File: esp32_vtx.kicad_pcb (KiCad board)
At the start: 4 copper layers, 20.1 x 23.3 mm, 33 parts, among them J1 Conn_01x24_MountingPin, J2 Conn_01x05, U1 AMS1117-3.3, U2 ESP-PSRAM32, U3 ESP32-PICO-D4, U4 MKDV4GCL-AB, U5 XC6206PxxxMR, U6 XC6206PxxxMR

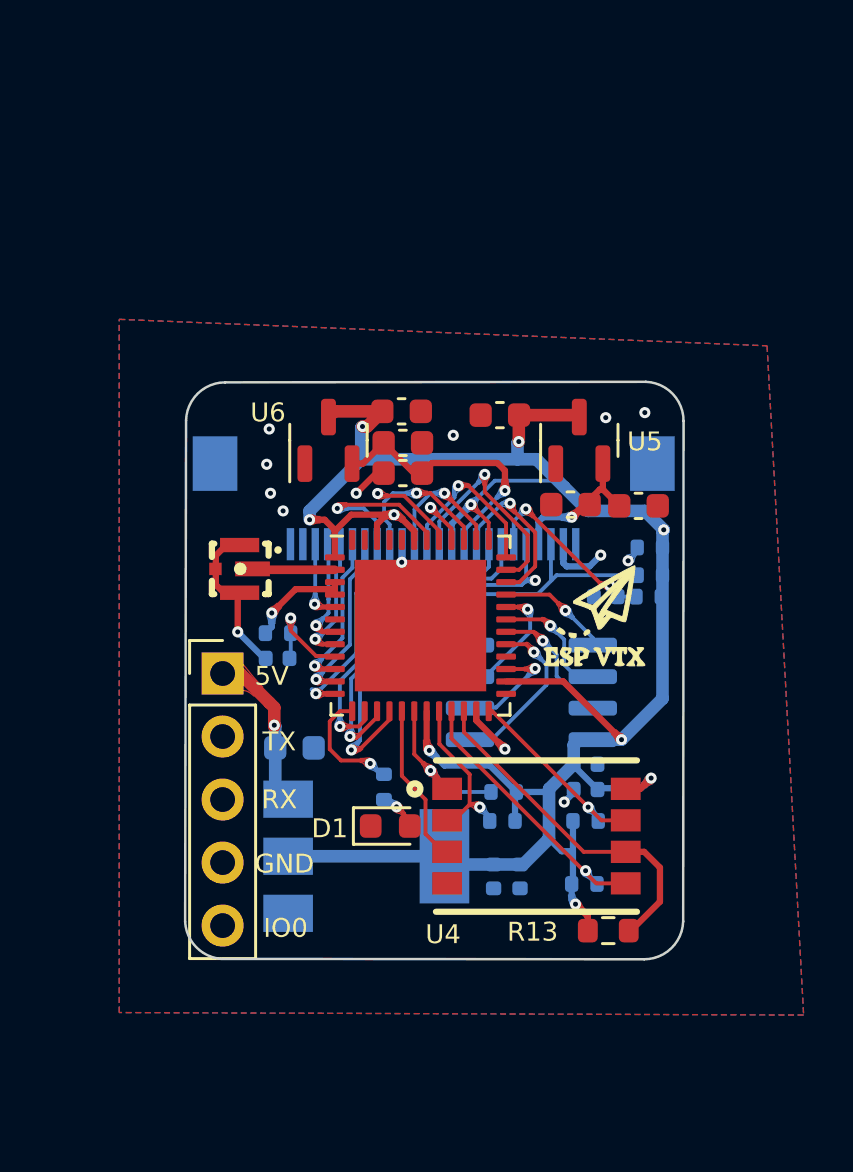
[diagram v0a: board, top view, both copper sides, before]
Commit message: add cap near pclk, change package of res and cap to 0603
Signed-off-by: huangzzk <huangcmzzk@gmail.com>
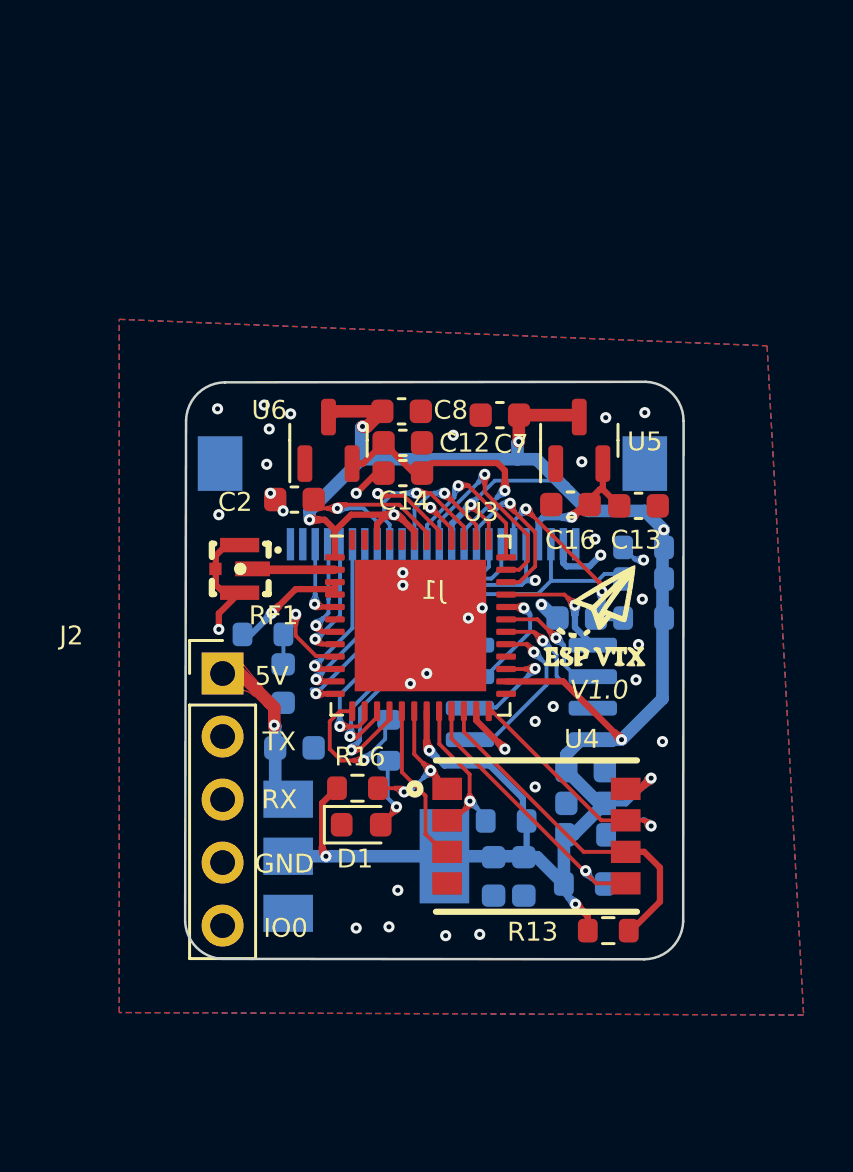
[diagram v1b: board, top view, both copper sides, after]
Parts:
- added C2: 0.1uF, Capacitor_SMD:C_0603_1608Metric, F.Cu at (126.7, 92.4)
- C10, C11, C15, C5, C6, C9: footprint Capacitor_SMD:C_0402_1005Metric -> Capacitor_SMD:C_0603_1608Metric
- R1, R11, R12, R14, R15, R17, R18, R9: footprint Resistor_SMD:R_0402_1005Metric -> Resistor_SMD:R_0603_1608Metric
- R16: footprint Resistor_SMD:R_0402_1005Metric -> Resistor_SMD:R_0603_1608Metric; moved to F.Cu
- U2: value ESP-PSRAM32 -> IS25WP032
- U5: value XC6206PxxxMR -> XC6206-2.8V
- U6: value XC6206PxxxMR -> XC6206-1.2V
- moved R16 5.89 mm to (129.2, 104.0), turned to 0 degrees
- moved R12 1.89 mm to (130.5, 102.1)
- moved C9 1.45 mm to (138.1, 97.1)
- moved D1 1.17 mm to (129.4, 105.5)
- moved C11 1.04 mm to (126.2, 99.8), turned to -90 degrees
- moved R1 0.89 mm to (140.8, 97.1)
- moved R11 0.61 mm to (125.4, 97.8)
- moved C15 0.56 mm to (138.4, 104.6)
- moved R15 0.56 mm to (138.4, 105.9)
- moved R9 0.30 mm to (140.8, 95.6)
- moved R14 0.25 mm to (140.8, 94.3)
- moved C10 0.25 mm to (138.4, 103.3)
- moved C5 0.15 mm to (135.9, 107.5)
- moved R17 0.15 mm to (135.2, 105.3)
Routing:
- net +3V3: track 104.9 -> 108.3 mm, vias 11 -> 12
- net /SD_DATA1: track 8.07 -> 10.6 mm
- net /SDA: track 20.7 -> 18.2 mm
- net /VS: track 13.9 -> 12.1 mm
- net Net-(D1-Pad2): track 1.41 -> 3.12 mm
- net /PWDN: track 12.3 -> 10.9 mm
- net /SCL: track 20.7 -> 19.5 mm
- net /PCLK: track 7.17 -> 8.27 mm
- net Net-(R12-Pad1): track 4.80 -> 5.82 mm
- net /EN: track 4.37 -> 5.28 mm
- net /RESET: track 7.61 -> 8.49 mm
- net GND: track 12.3 -> 11.6 mm, vias 12 -> 34
- net /SD_DATA2: track 6.47 -> 6.22 mm, vias 1 -> 2
- net (no net): vias 0 -> 1
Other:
- board text added: "V1.0"

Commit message: v1.1 tested.
Signed-off-by: huangzzk <huangcmzzk@gmail.com>
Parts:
- removed C6: 0.1uF, Capacitor_SMD:C_0603_1608Metric
- added C3: 100uF, Capacitor_Tantalum_SMD:CP_EIA-3216-18_Kemet-A, B.Cu at (137.9, 107.7)
- added R2: 0R, Resistor_SMD:R_0603_1608Metric, F.Cu at (123.9, 108.9)
- added R3: 0R, Resistor_SMD:R_0603_1608Metric, B.Cu at (123.9, 109.2)
- added SW1: SW_SPST, Button_Switch_SMD:SW_SPST_B3U-1000P, F.Cu at (128.2, 109.1)
- added SW2: SW_SPST, Button_Switch_SMD:SW_SPST_B3U-1000P, F.Cu at (128.2, 106.1)
- C2: value 0.1uF -> 15pF; moved to B.Cu
- J2: value Conn_01x05 -> Conn_01x04; footprint Connector_PinHeader_2.54mm:PinHeader_1x05_P2.54mm_Vertical -> Connector_PinHeader_2.54mm:PinHeader_1x04_P2.54mm_Vertical
- R13, R16: moved to B.Cu
- moved C2 5.61 mm to (131.1, 95.8), turned to 0 degrees
- moved D1 3.04 mm to (126.8, 103.8)
- moved R16 2.99 mm to (131.5, 102.1), turned to -90 degrees
- moved R15 2.24 mm to (140.6, 106.4)
- moved R18 2.24 mm to (140.6, 107.9)
- moved R13 1.31 mm to (140.6, 109.4)
- moved C14 0.56 mm to (131.1, 90.7), turned to 0 degrees
- moved C12 0.46 mm to (131.1, 89.6)
- moved R12 0.46 mm to (130.0, 102.1)
- moved U6 0.46 mm to (128.1, 89.5)
- moved C8 0.36 mm to (131.0, 88.4)
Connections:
- C12 pad 2: GND -> GNDD
- C13 pad 2: GND -> GNDA
- C14 pad 2: GND -> GNDD
- C16 pad 2: GND -> GNDA
- C2 pad 2: GND -> GNDD
- J1 pad 10: GND -> GNDD
- J1 pad 23: GND -> GNDA
- U5 pad 1: GND -> GNDA
- U6 pad 1: GND -> GNDD
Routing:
- net GNDA: track 0.00 -> 37.4 mm, vias 0 -> 2
- net GNDD: track 0.00 -> 31.7 mm, vias 0 -> 2
- net /SD_DATA0: track 14.1 -> 24.5 mm, vias 0 -> 1
- net /GPIO0: track 16.3 -> 8.40 mm, vias 1 -> 2
- net +3V3: track 108.3 -> 104.8 mm, vias 12 -> 8
- net /D7: track 6.26 -> 8.53 mm
- net +1V2: track 11.0 -> 13.0 mm, vias 1 -> 2
- net /SD_DATA2: track 6.22 -> 4.44 mm, vias 2 -> 1
- net /PCLK: track 8.27 -> 9.60 mm, vias 1 -> 2
- net /D8: track 5.30 -> 6.63 mm
- net /TX: track 17.4 -> 18.7 mm
- net /SCL: track 19.5 -> 20.7 mm
- net /SD_CMD: track 11.3 -> 12.5 mm
- net /SD_DATA1: track 10.6 -> 9.48 mm
- net /D6: track 7.05 -> 8.07 mm
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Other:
- board text added: "G"
- board text added: "R"
- board text added: "T"
- board text added: "V1.1"
- board text removed: "GND"
- board text removed: "IO0"
- board text removed: "RX"
- board text removed: "TX"
- board text removed: "V1.0"

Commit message: update
Signed-off-by: huangzzk <huangcmzzk@gmail.com>
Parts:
- removed R2, R3: 0R, Resistor_SMD:R_0603_1608Metric
- added ?: , , F.Cu at (132.4, 78.9)
- added C17: 10u, Capacitor_SMD:C_0603_1608Metric, F.Cu at (130.7, 92.0)
- added C18: 10u, Capacitor_SMD:C_0603_1608Metric, F.Cu at (135.3, 92.2)
- added C19: 10u, Capacitor_SMD:C_0603_1608Metric, B.Cu at (127.5, 90.8)
- added C4: 10u, Capacitor_SMD:C_0603_1608Metric, F.Cu at (126.9, 93.0)
- added C6: 10u, Capacitor_SMD:C_0603_1608Metric, F.Cu at (129.0, 92.0)
- added H1: MountingHole, MountingHole:MountingHole_2.2mm_M2, F.Cu at (124.4, 111.4)
- added H2: MountingHole, MountingHole:MountingHole_2.2mm_M2, F.Cu at (124.4, 87.7)
- added H3: MountingHole, MountingHole:MountingHole_2.2mm_M2, F.Cu at (140.3, 111.2)
- added H4: MountingHole, MountingHole:MountingHole_2.2mm_M2, F.Cu at (140.3, 87.7)
- R11, R14, R15, R18: moved to F.Cu
- RF1: value KH-IPEX4-2020 -> BWIPX-1-001E; footprint ic_footprint:IPEX4-SMD_4P-L1.8-W1.7-LS2.0-L_KH-IPEX4-2020 -> kicad_lceda:IPEX-SMD_BWIPX-1-001E
- moved R14 14.8 mm to (128.9, 103.1), turned to 0 degrees
- moved R9 14.2 mm to (130.2, 105.1), turned to 0 degrees
- moved C15 9.41 mm to (134.2, 113.0), turned to 180 degrees
- moved R17 8.03 mm to (127.3, 106.3)
- moved SW1 7.10 mm to (134.7, 112.0)
- moved SW2 5.94 mm to (129.5, 111.9)
- moved C2 5.63 mm to (128.6, 100.8), turned to 180 degrees
- moved C9 5.55 mm to (141.6, 101.4), turned to -90 degrees
- moved R16 5.21 mm to (127.3, 105.1), turned to 180 degrees
- moved U4 4.82 mm to (131.7, 106.9)
- moved J1 4.62 mm to (132.2, 96.9)
- moved C5 4.59 mm to (136.4, 112.1)
- moved R13 4.22 mm to (136.4, 109.3), turned to 90 degrees
- moved U1 3.84 mm to (130.9, 110.3)
- moved C10 3.33 mm to (141.6, 104.2), turned to -90 degrees
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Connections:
- net /SD_DATA0 renamed /GPIO2
- C12 pad 2: GNDD -> GND
- C13 pad 2: GNDA -> GND
- C14 pad 2: GNDD -> GND
- C16 pad 2: GNDA -> GND
- C2 pad 2: GNDD -> GND
- J1 pad 10: GNDD -> GND
- J1 pad 23: GNDA -> GND
- U5 pad 1: GNDA -> GND
- U6 pad 1: GNDD -> GND
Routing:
- net GNDA: track 37.4 -> 0.00 mm, vias 2 -> 0
- net GNDD: track 31.7 -> 0.00 mm, vias 2 -> 0
- net +3V3: track 104.8 -> 121.8 mm, vias 8 -> 13
- net /GPIO2: track 24.5 -> 14.6 mm, vias 1 -> 2
- net /SIO2: track 4.25 -> 11.9 mm, vias 1 -> 3
- net /SCL: track 20.7 -> 13.7 mm, vias 3 -> 1
- net /D9: track 8.80 -> 15.3 mm
- net /PCLK: track 9.60 -> 15.5 mm
- net GND: track 12.6 -> 18.4 mm, vias 20 -> 24
- net /SO: track 3.73 -> 9.33 mm, vias 1 -> 3
- net /RESET: track 8.15 -> 13.5 mm
- net +5V: track 6.58 -> 11.7 mm
- net /MCLK: track 7.17 -> 12.1 mm, vias 1 -> 2
- net /GPIO0: track 8.40 -> 13.1 mm
- net /SCLK: track 4.22 -> 8.96 mm
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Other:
- board size 20.1 x 23.3 mm -> 20.1 x 39.6 mm
- board text added: "V2.1"
- board text removed: "V1.1"
